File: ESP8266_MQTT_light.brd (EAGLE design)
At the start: 68.6 x 68.6 mm, 29 parts, among them IC2 7805DT, J1 DCJ0202, J2 RGBW1, Q1 IRF3704S, Q2 IRF3704S, Q3 IRF3704S, Q4 IRF3704S, SW1 2-1825910-7, SW2 2-1825910-7, SW3 2-1825910-7

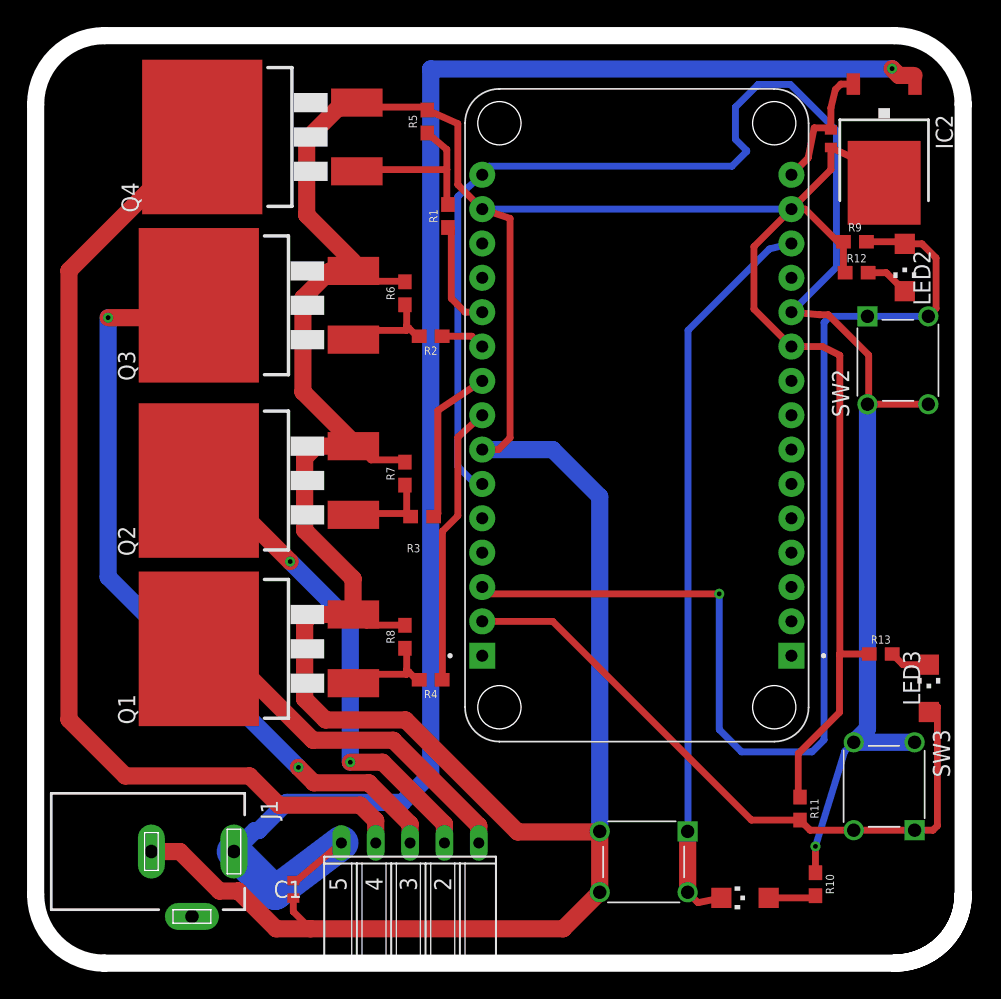
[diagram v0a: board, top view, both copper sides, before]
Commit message: Changed Switch on board
The original board had an error on the switch
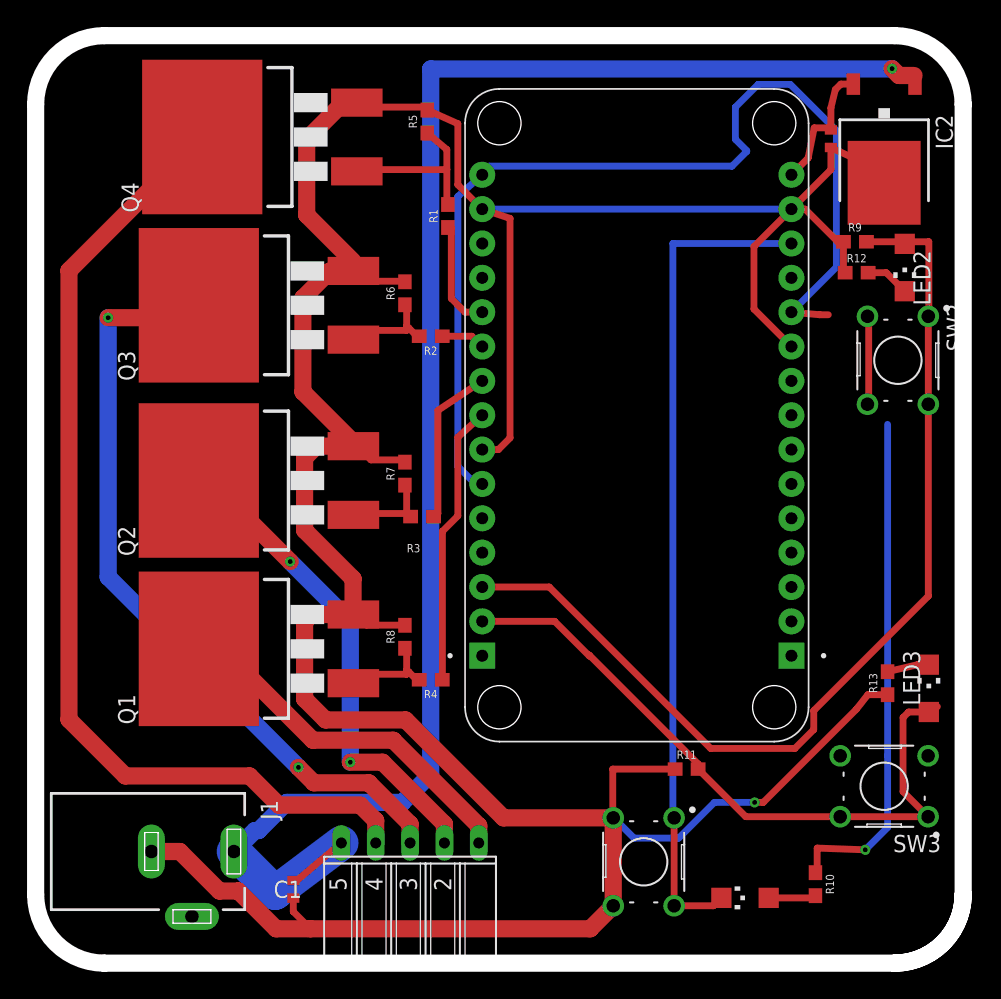
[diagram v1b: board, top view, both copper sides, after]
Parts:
- SW1, SW2, SW3: value 2-1825910-7 -> B3F-1000; device Switch:2-1825910-7 -> Switch:B3F-1000
- moved R11 8.88 mm to (48.1, 14.4), turned to 0 degrees
- moved R13 2.22 mm to (63.0, 20.7), turned to 90 degrees
- turned SW1 to 270 degrees
- turned SW2 to 270 degrees
- turned SW3 to 180 degrees
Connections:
- net M-CTL renamed N$5
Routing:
- net GND: track 307.5 -> 269.3 mm, vias 0 -> 1
- net N$5: track 86.3 -> 74.5 mm, vias 1 -> 0
- net 3.3VDC: track 128.3 -> 120.7 mm
- net RESET: track 54.6 -> 61.5 mm

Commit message: Changed Resistor footprint
I changed the resistors to a 1206 SMD footprint
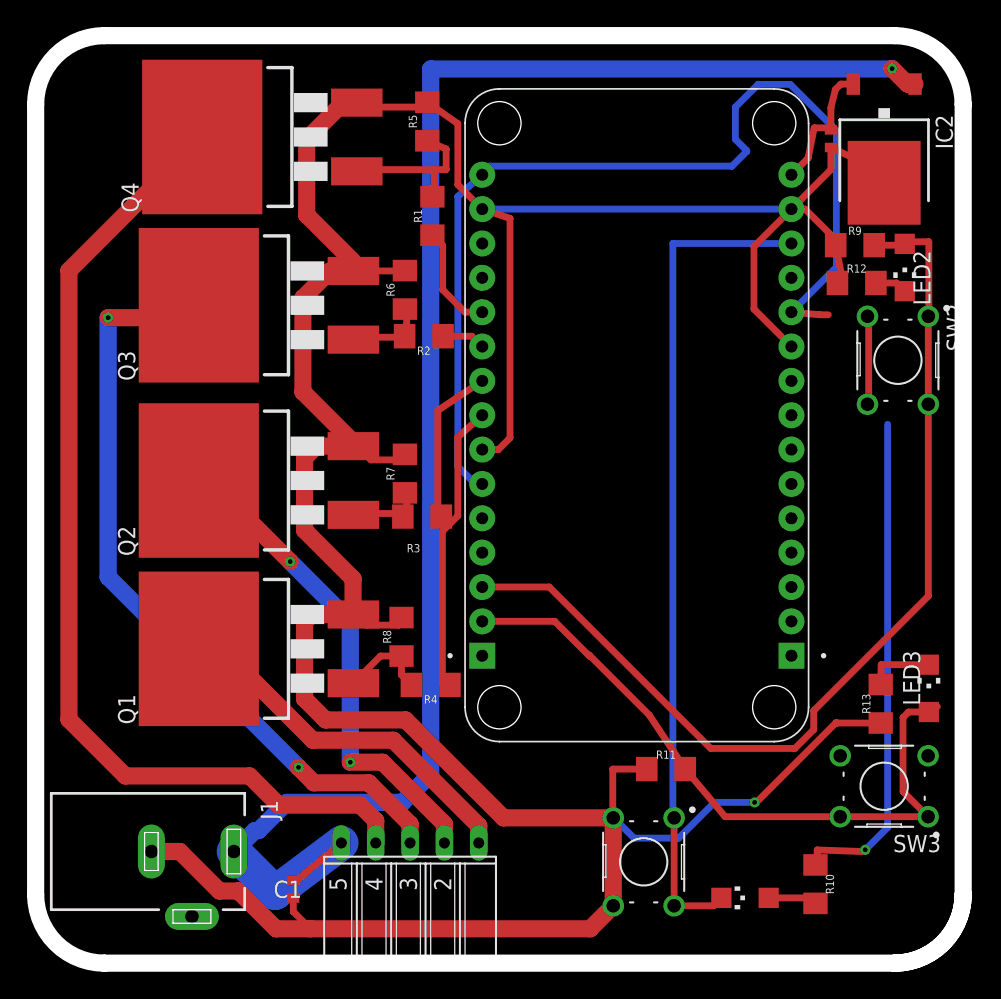
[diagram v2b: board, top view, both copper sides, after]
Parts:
- R1, R10, R11, R12, R13, R2, R3, R4, R5, R6, R7, R8, R9: device SparkFun-Resistors:0603 -> rcl:R1206
- moved R13 1.61 mm to (62.5, 19.2)
- moved R11 1.52 mm to (46.6, 14.4)
- moved R1 1.14 mm to (29.3, 55.2)
- moved R12 0.76 mm to (60.7, 50.3)
- moved R2 0.51 mm to (28.7, 46.4)
- moved R4 0.38 mm to (29.2, 20.6)
- moved R9 0.25 mm to (60.6, 53.1)
- moved R8 0.25 mm to (27.1, 24.1)
- moved R6 0.25 mm to (27.3, 49.8)
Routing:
- net GND: track 269.3 -> 267.4 mm
- net N$3: track 3.11 -> 4.99 mm
- net W-IN: track 7.27 -> 8.38 mm
- net R-IN: track 12.7 -> 11.6 mm
- net N$2: track 3.27 -> 2.39 mm
- net W-MAIN: track 20.8 -> 21.7 mm

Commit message: Board corrections
Corrected amended board to allo for the larger 1206 resistors
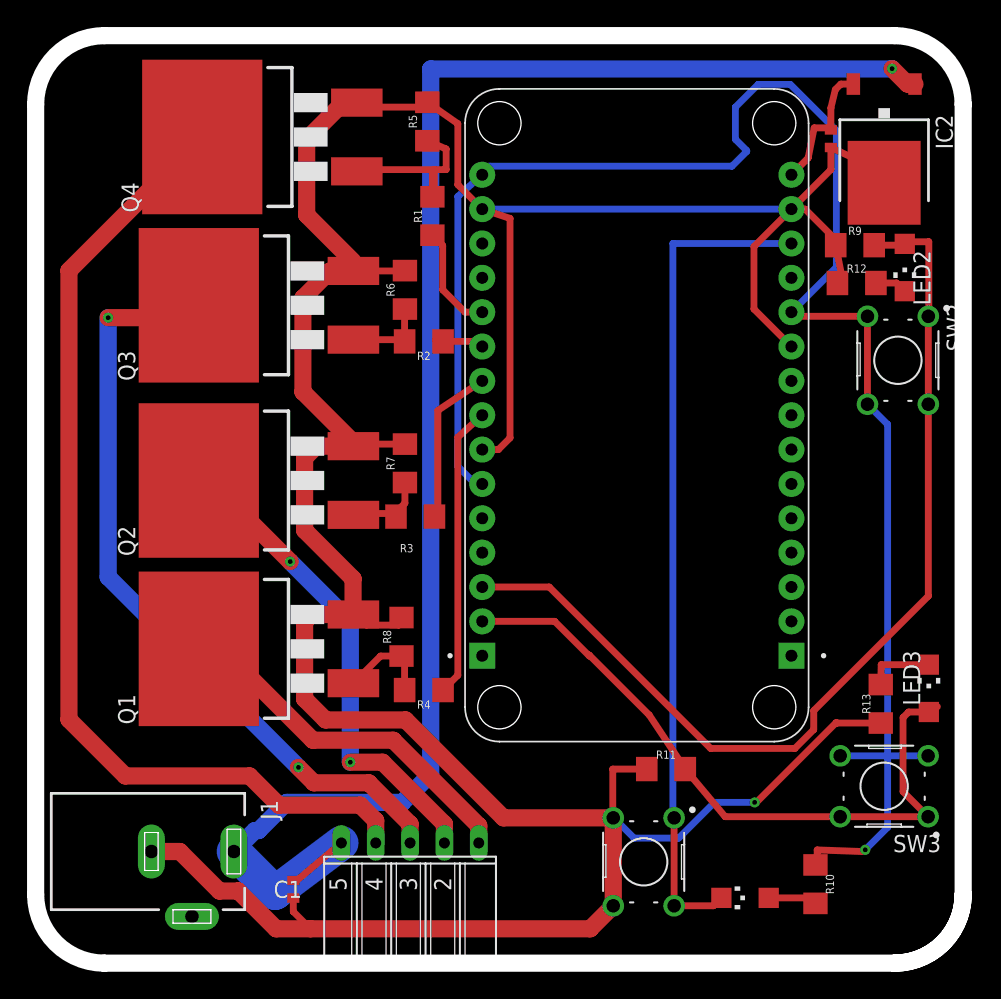
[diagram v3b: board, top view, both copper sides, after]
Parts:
- moved R7 0.76 mm to (27.3, 37.0)
- moved R4 0.63 mm to (28.7, 20.2)
- moved R3 0.51 mm to (28.1, 33.0)
- moved R2 0.38 mm to (28.7, 46.0)
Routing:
- net 3.3VDC: track 120.9 -> 131.7 mm
- net R-IN: track 11.6 -> 13.7 mm
- net GND: track 267.4 -> 266.8 mm
